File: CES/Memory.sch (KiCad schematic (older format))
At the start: 8 parts, among them U601 SST39SF020, U602 SST39SF020, U603 IS61C256, U604 IS61C256

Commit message: Control Unit
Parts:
- renumbered C601 to C1101, C602 to C1102, C603 to C1103, C604 to C1104, U601 to U1101, U602 to U1102, U603 to U1103, U604 to U1104
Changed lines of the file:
@@
 $Descr A4 8268 11693 portrait
 encoding utf-8
-Sheet 10 16
+Sheet 10 17
 Title "CES"
 Date "2021-04-24"
@@
 	3250 1800 3250 1900
 $Comp
-L power:GND #PWR0603
+L power:GND #PWR01103
 U 1 1 608579D0
 P 3250 3050
-F 0 "#PWR0603" H 3250 2800 50  0001 C CNN
+F 0 "#PWR01103" H 3250 2800 50  0001 C CNN
 F 1 "GND" H 3400 3000 50  0000 C CNN
 F 2 "" H 3250 3050 50  0001 C CNN
@@
 	4350 4750 4350 4700
 $Comp
-L power:GND #PWR0607
+L power:GND #PWR01107
 U 1 1 6085B823
 P 4350 4750
-F 0 "#PWR0607" H 4350 4500 50  0001 C CNN
+F 0 "#PWR01107" H 4350 4500 50  0001 C CNN
 F 1 "GND" H 4200 4700 50  0000 C CNN
 F 2 "" H 4350 4750 50  0001 C CNN
@@
 $EndComp
 $Comp
-L CES:IS61C256 U603
+L CES:IS61C256 U1103
 U 1 1 60841D0E
 P 4850 4200
-F 0 "U603" H 4850 3450 50  0000 L CNN
+F 0 "U1103" H 4850 3450 50  0000 L CNN
 F 1 "IS61C256" H 4750 3300 50  0000 L CNN
 F 2 "" H 1900 2750 50  0001 C CNN
@@
 $EndComp
 $Comp
-L Memory_Flash:SST39SF020 U601
+L Memory_Flash:SST39SF020 U1101
 U 1 1 60833BBD
 P 4750 1900
-F 0 "U601" H 4800 1000 50  0000 L CNN
+F 0 "U1101" H 4800 1000 50  0000 L CNN
 F 1 "SST39SF020" H 4650 850 50  0000 L CNN
 F 2 "" H 4750 2200 50  0001 C CNN
@@
 	6600 700  7500 700
 $Comp
-L power:GND #PWR0608
+L power:GND #PWR01108
 U 1 1 60880C69
 P 4350 9400
-F 0 "#PWR0608" H 4350 9150 50  0001 C CNN
+F 0 "#PWR01108" H 4350 9150 50  0001 C CNN
 F 1 "GND" H 4200 9350 50  0000 C CNN
 F 2 "" H 4350 9400 50  0001 C CNN
@@
 Connection ~ 2150 5350
 $Comp
-L Device:C C601
+L Device:C C1101
 U 1 1 60C3CB73
 P 1100 10350
-F 0 "C601" H 1150 10450 50  0000 L CNN
+F 0 "C1101" H 1150 10450 50  0000 L CNN
 F 1 "100nF" H 1150 10250 50  0000 L CNN
 F 2 "" H 1138 10200 50  0001 C CNN
@@
 $EndComp
 $Comp
-L Device:C C602
+L Device:C C1102
 U 1 1 60C83B06
 P 1400 10350
-F 0 "C602" H 1450 10450 50  0000 L CNN
+F 0 "C1102" H 1450 10450 50  0000 L CNN
 F 1 "100nF" H 1450 10250 50  0000 L CNN
 F 2 "" H 1438 10200 50  0001 C CNN
@@
 $EndComp
 $Comp
-L Device:C C603
+L Device:C C1103
 U 1 1 60C91C93
 P 1650 10350
-F 0 "C603" H 1700 10450 50  0000 L CNN
+F 0 "C1103" H 1700 10450 50  0000 L CNN
 F 1 "100nF" H 1700 10250 50  0000 L CNN
 F 2 "" H 1688 10200 50  0001 C CNN
@@
 $EndComp
 $Comp
-L Device:C C604
+L Device:C C1104
 U 1 1 60C9FE20
 P 1900 10350
-F 0 "C604" H 1950 10450 50  0000 L CNN
+F 0 "C1104" H 1950 10450 50  0000 L CNN
 F 1 "100nF" H 1950 10250 50  0000 L CNN
 F 2 "" H 1938 10200 50  0001 C CNN
@@
 $EndComp
 $Comp
-L power:GND #PWR0602
+L power:GND #PWR01101
 U 1 1 60CADC4B
 P 1550 10750
-F 0 "#PWR0602" H 1550 10500 50  0001 C CNN
+F 0 "#PWR01101" H 1550 10500 50  0001 C CNN
 F 1 "GND" H 1555 10577 50  0000 C CNN
 F 2 "" H 1550 10750 50  0001 C CNN
@@
 $EndComp
 $Comp
-L power:VCC #PWR0601
+L power:VCC #PWR01102
 U 1 1 60CAE784
 P 1600 10050
-F 0 "#PWR0601" H 1600 9900 50  0001 C CNN
+F 0 "#PWR01102" H 1600 9900 50  0001 C CNN
 F 1 "VCC" H 1615 10223 50  0000 C CNN
 F 2 "" H 1600 10050 50  0001 C CNN
@@
 	1550 10600 1650 10600
 $Comp
-L power:VCC #PWR0605
+L power:VCC #PWR01105
 U 1 1 60D39965
 P 3950 2650
-F 0 "#PWR0605" H 3950 2500 50  0001 C CNN
+F 0 "#PWR01105" H 3950 2500 50  0001 C CNN
 F 1 "VCC" H 4050 2700 50  0000 C CNN
 F 2 "" H 3950 2650 50  0001 C CNN
@@
 	3250 6450 3250 6550
 $Comp
-L power:GND #PWR0604
+L power:GND #PWR01104
 U 1 1 60E7C27B
 P 3250 7700
-F 0 "#PWR0604" H 3250 7450 50  0001 C CNN
+F 0 "#PWR01104" H 3250 7450 50  0001 C CNN
 F 1 "GND" H 3400 7650 50  0000 C CNN
 F 2 "" H 3250 7700 50  0001 C CNN
@@
 Connection ~ 3250 7150
 $Comp
-L power:VCC #PWR0606
+L power:VCC #PWR01106
 U 1 1 60E7C282
 P 3950 7300
-F 0 "#PWR0606" H 3950 7150 50  0001 C CNN
+F 0 "#PWR01106" H 3950 7150 50  0001 C CNN
 F 1 "VCC" H 4050 7350 50  0000 C CNN
 F 2 "" H 3950 7300 50  0001 C CNN
@@
 	3850 9750 4450 9750
 $Comp
-L power:GND #PWR0103
+L power:GND #PWR01111
 U 1 1 60F0D21B
 P 4400 7750
-F 0 "#PWR0103" H 4400 7500 50  0001 C CNN
+F 0 "#PWR01111" H 4400 7500 50  0001 C CNN
 F 1 "GND" H 4550 7700 50  0000 C CNN
 F 2 "" H 4400 7750 50  0001 C CNN
@@
 $EndComp
 $Comp
-L power:GND #PWR0104
+L power:GND #PWR01114
 U 1 1 60F0D703
 P 4850 5150
-F 0 "#PWR0104" H 4850 4900 50  0001 C CNN
+F 0 "#PWR01114" H 4850 4900 50  0001 C CNN
 F 1 "GND" H 5000 5100 50  0000 C CNN
 F 2 "" H 4850 5150 50  0001 C CNN
@@
 $EndComp
 $Comp
-L CES:IS61C256 U604
+L CES:IS61C256 U1104
 U 1 1 6083E55E
 P 4850 8850
-F 0 "U604" H 4850 8100 50  0000 L CNN
+F 0 "U1104" H 4850 8100 50  0000 L CNN
 F 1 "IS61C256" H 4750 7950 50  0000 L CNN
 F 2 "" H 1900 7400 50  0001 C CNN
@@
 $EndComp
 $Comp
-L power:GND #PWR0105
+L power:GND #PWR01116
 U 1 1 60F39577
 P 4850 9800
-F 0 "#PWR0105" H 4850 9550 50  0001 C CNN
+F 0 "#PWR01116" H 4850 9550 50  0001 C CNN
 F 1 "GND" H 5000 9700 50  0000 C CNN
 F 2 "" H 4850 9800 50  0001 C CNN
@@
 $EndComp
 $Comp
-L power:VCC #PWR0106
+L power:VCC #PWR01112
 U 1 1 60F73B80
 P 4750 600
-F 0 "#PWR0106" H 4750 450 50  0001 C CNN
+F 0 "#PWR01112" H 4750 450 50  0001 C CNN
 F 1 "VCC" H 4900 650 50  0000 C CNN
 F 2 "" H 4750 600 50  0001 C CNN
@@
 $EndComp
 $Comp
-L power:VCC #PWR0107
+L power:VCC #PWR01115
 U 1 1 60F74E71
 P 4850 7850
-F 0 "#PWR0107" H 4850 7700 50  0001 C CNN
+F 0 "#PWR01115" H 4850 7700 50  0001 C CNN
 F 1 "VCC" H 4950 7900 50  0000 C CNN
 F 2 "" H 4850 7850 50  0001 C CNN
@@
 $EndComp
 $Comp
-L power:VCC #PWR0108
+L power:VCC #PWR01113
 U 1 1 60F75552
 P 4850 3200
-F 0 "#PWR0108" H 4850 3050 50  0001 C CNN
+F 0 "#PWR01113" H 4850 3050 50  0001 C CNN
 F 1 "VCC" H 4950 3250 50  0000 C CNN
 F 2 "" H 4850 3200 50  0001 C CNN
@@
 $EndComp
 $Comp
-L Memory_Flash:SST39SF020 U602
+L Memory_Flash:SST39SF020 U1102
 U 1 1 60837E5F
 P 4750 6550
-F 0 "U602" H 4750 5650 50  0000 L CNN
+F 0 "U1102" H 4750 5650 50  0000 L CNN
 F 1 "SST39SF020" H 4650 5500 50  0000 L CNN
 F 2 "" H 4750 6850 50  0001 C CNN
@@
 $EndComp
 $Comp
-L power:VCC #PWR0109
+L power:VCC #PWR01110
 U 1 1 60F95BCF
 P 4400 5250
-F 0 "#PWR0109" H 4400 5100 50  0001 C CNN
+F 0 "#PWR01110" H 4400 5100 50  0001 C CNN
 F 1 "VCC" H 4500 5300 50  0000 C CNN
 F 2 "" H 4400 5250 50  0001 C CNN
@@
 	4400 5250 4750 5250
 $Comp
-L power:GND #PWR0110
+L power:GND #PWR01109
 U 1 1 60FA9AB5
 P 4400 3100
-F 0 "#PWR0110" H 4400 2850 50  0001 C CNN
+F 0 "#PWR01109" H 4400 2850 50  0001 C CNN
 F 1 "GND" H 4550 3050 50  0000 C CNN
 F 2 "" H 4400 3100 50  0001 C CNN

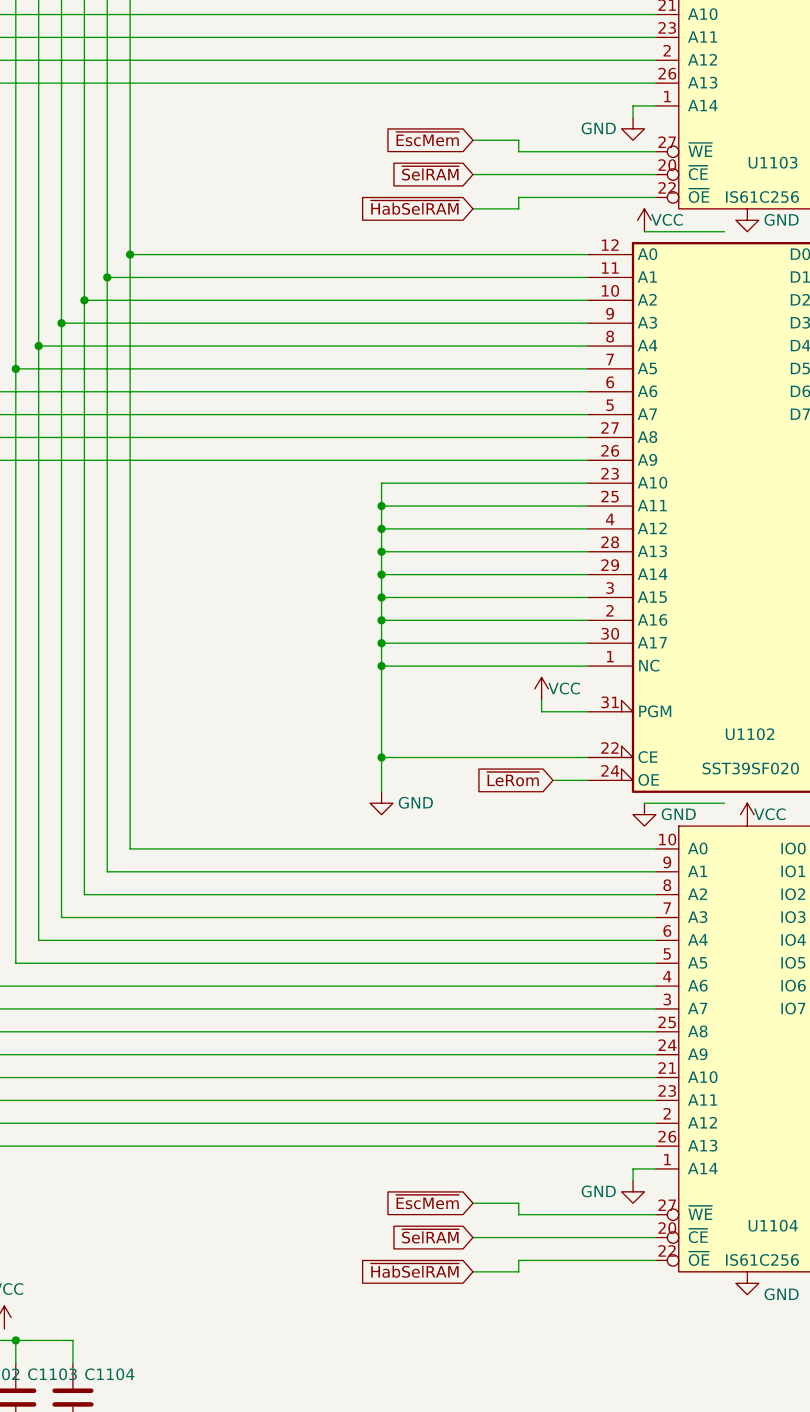
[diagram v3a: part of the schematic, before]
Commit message: Correcting ERC issues
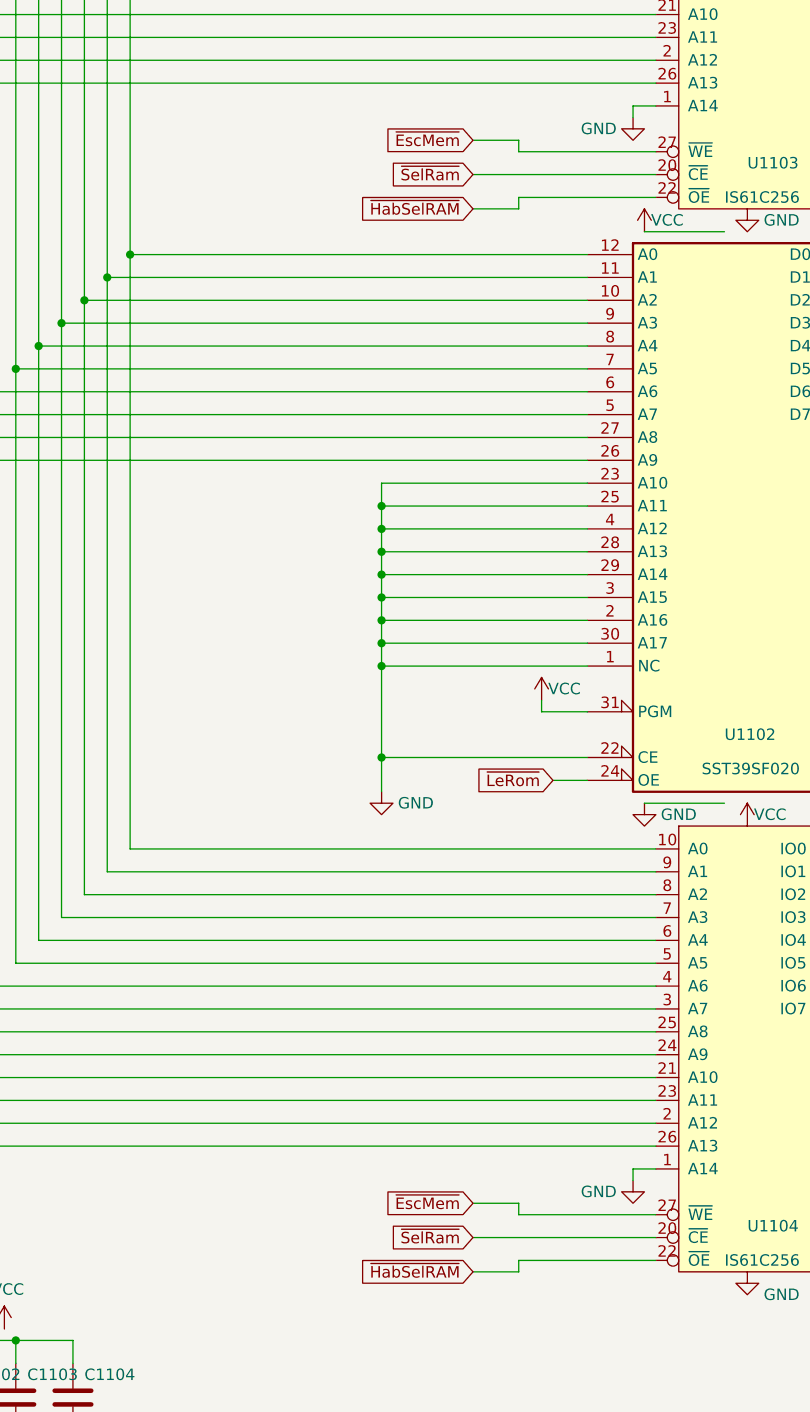
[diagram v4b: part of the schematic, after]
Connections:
- net ~SelRAM renamed ~SelRam
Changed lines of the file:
@@
 $Descr A4 8268 11693 portrait
 encoding utf-8
-Sheet 10 17
+Sheet 11 18
 Title "CES"
 Date "2021-04-24"
@@
 ~EscMem
 Text GLabel 3650 5000 0    50   Input ~ 0
-~SelRAM
+~SelRam
 Text GLabel 3650 5150 0    50   Input ~ 0
 ~HabSelRAM
@@
 ~EscMem
 Text GLabel 3650 9650 0    50   Input ~ 0
-~SelRAM
+~SelRam
 Text GLabel 3650 9800 0    50   Input ~ 0
 ~HabSelRAM

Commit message: Assigning footprints and generating netlist
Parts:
- C1101, C1102, C1103, C1104: footprint (none) -> Capacitor_THT:CP_Radial_D5.0mm_P2.50mm
- U1101, U1102: footprint (none) -> Package_DIP:DIP-32_W15.24mm_Socket
- U1103, U1104: footprint (none) -> Package_DIP:DIP-28_W7.62mm
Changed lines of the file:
@@
 F 0 "U1103" H 4850 3450 50  0000 L CNN
 F 1 "IS61C256" H 4750 3300 50  0000 L CNN
-F 2 "" H 1900 2750 50  0001 C CNN
+F 2 "Package_DIP:DIP-28_W7.62mm" H 1900 2750 50  0001 C CNN
 F 3 "" H 1900 2750 50  0001 C CNN
 	1    4850 4200
@@
 F 0 "U1101" H 4800 1000 50  0000 L CNN
 F 1 "SST39SF020" H 4650 850 50  0000 L CNN
-F 2 "" H 4750 2200 50  0001 C CNN
+F 2 "Package_DIP:DIP-32_W15.24mm_Socket" H 4750 2200 50  0001 C CNN
 F 3 "http://ww1.microchip.com/downloads/en/DeviceDoc/25022B.pdf" H 4750 2200 50  0001 C CNN
 	1    4750 1900
@@
 F 0 "C1101" H 1150 10450 50  0000 L CNN
 F 1 "100nF" H 1150 10250 50  0000 L CNN
-F 2 "" H 1138 10200 50  0001 C CNN
+F 2 "Capacitor_THT:CP_Radial_D5.0mm_P2.50mm" H 1138 10200 50  0001 C CNN
 F 3 "~" H 1100 10350 50  0001 C CNN
 	1    1100 10350
@@
 F 0 "C1102" H 1450 10450 50  0000 L CNN
 F 1 "100nF" H 1450 10250 50  0000 L CNN
-F 2 "" H 1438 10200 50  0001 C CNN
+F 2 "Capacitor_THT:CP_Radial_D5.0mm_P2.50mm" H 1438 10200 50  0001 C CNN
 F 3 "~" H 1400 10350 50  0001 C CNN
 	1    1400 10350
@@
 F 0 "C1103" H 1700 10450 50  0000 L CNN
 F 1 "100nF" H 1700 10250 50  0000 L CNN
-F 2 "" H 1688 10200 50  0001 C CNN
+F 2 "Capacitor_THT:CP_Radial_D5.0mm_P2.50mm" H 1688 10200 50  0001 C CNN
 F 3 "~" H 1650 10350 50  0001 C CNN
 	1    1650 10350
@@
 F 0 "C1104" H 1950 10450 50  0000 L CNN
 F 1 "100nF" H 1950 10250 50  0000 L CNN
-F 2 "" H 1938 10200 50  0001 C CNN
+F 2 "Capacitor_THT:CP_Radial_D5.0mm_P2.50mm" H 1938 10200 50  0001 C CNN
 F 3 "~" H 1900 10350 50  0001 C CNN
 	1    1900 10350
@@
 F 0 "U1104" H 4850 8100 50  0000 L CNN
 F 1 "IS61C256" H 4750 7950 50  0000 L CNN
-F 2 "" H 1900 7400 50  0001 C CNN
+F 2 "Package_DIP:DIP-28_W7.62mm" H 1900 7400 50  0001 C CNN
 F 3 "" H 1900 7400 50  0001 C CNN
 	1    4850 8850
@@
 F 0 "U1102" H 4750 5650 50  0000 L CNN
 F 1 "SST39SF020" H 4650 5500 50  0000 L CNN
-F 2 "" H 4750 6850 50  0001 C CNN
+F 2 "Package_DIP:DIP-32_W15.24mm_Socket" H 4750 6850 50  0001 C CNN
 F 3 "http://ww1.microchip.com/downloads/en/DeviceDoc/25022B.pdf" H 4750 6850 50  0001 C CNN
 	1    4750 6550
